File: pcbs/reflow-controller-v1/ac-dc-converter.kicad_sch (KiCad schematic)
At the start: 22 parts, among them U201 TPS62933DRLR

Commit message: footprint assignement fixed; buzzer added
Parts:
- C201: footprint (none) -> Capacitor_SMD:C_0603_1608Metric
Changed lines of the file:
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@@
 			)
 		)
-		(property "Footprint" ""
+		(property "Footprint" "Capacitor_SMD:C_0603_1608Metric"
 			(at 141.9352 43.18 0)
 			(effects

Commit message: WIP pcb design & routing
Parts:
- added D1: SMAJ5.0CA, Diode_SMD:D_SMA, symbol Device:D_TVS
- added J2: PinHeader 1x02 P2.54mm, Connector_PinHeader_2.54mm:PinHeader_1x02_P2.54mm_Vertical, symbol Connector_Generic:Conn_01x02
- added Q1: PMV65XP, Package_TO_SOT_SMD:SOT-23, symbol Device:Q_PMOS_GSD
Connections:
- net +5V: now also Q1.2 (S)
- net GND: now also D1.1 (A1), J2.2 (Pin_2), Q1.1 (G)
- new net: D1.2 (A2), J2.1 (Pin_1), Q1.3 (D)
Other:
- note added: "Debug Power In"

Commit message: update debug power footprint
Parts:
- J2: footprint Connector_PinHeader_2.54mm:PinHeader_1x02_P2.54mm_Vertical -> Connector_Molex:Molex_KK-254_AE-6410-02A_1x02_P2.54mm_Vertical
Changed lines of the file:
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@@
 			)
 		)
-		(property "Footprint" "Connector_PinHeader_2.54mm:PinHeader_1x02_P2.54mm_Vertical"
+		(property "Footprint" "Connector_Molex:Molex_KK-254_AE-6410-02A_1x02_P2.54mm_Vertical"
 			(at 43.18 160.02 0)
 			(effects

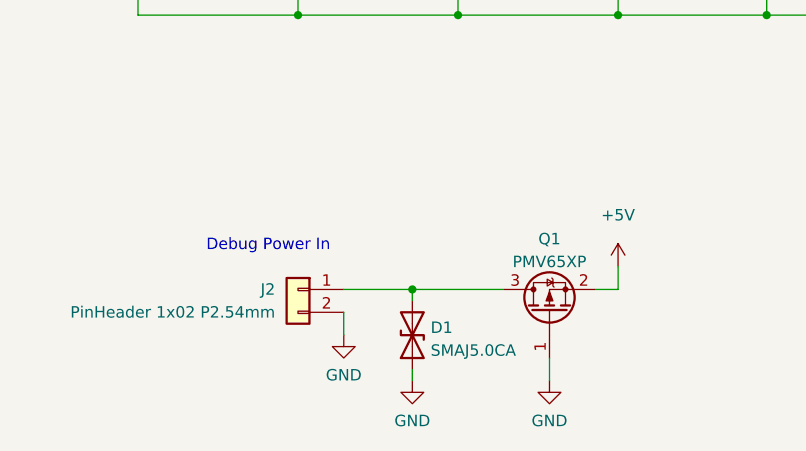
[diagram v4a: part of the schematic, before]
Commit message: add zero crossing detector
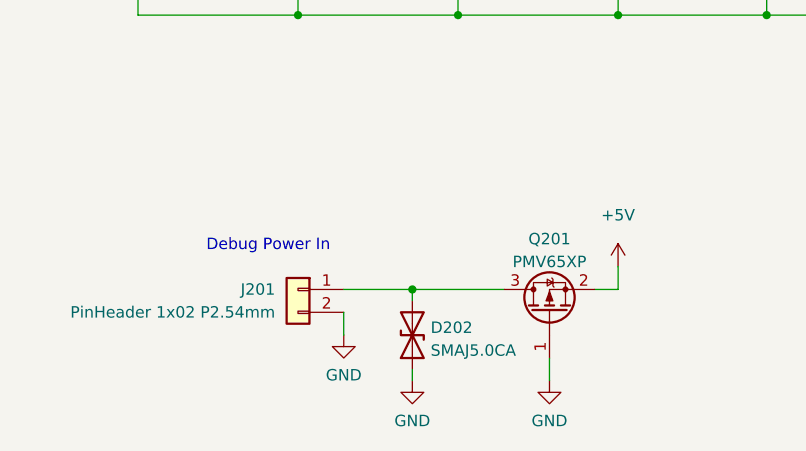
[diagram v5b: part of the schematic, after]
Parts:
- renumbered D1 to D202, J2 to J201, Q1 to Q201

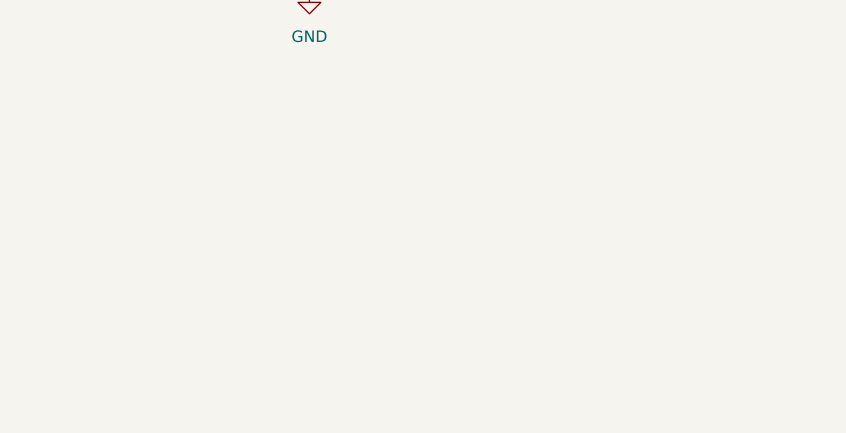
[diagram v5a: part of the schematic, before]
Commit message: add ldo for analog voltage
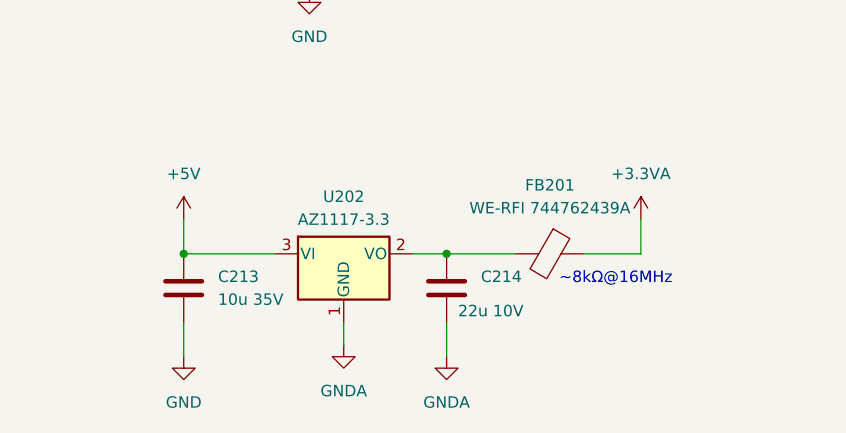
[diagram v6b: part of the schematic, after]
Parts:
- added C213: 10u 35V, Capacitor_SMD:C_1206_3216Metric, symbol Device:C
- added C214: 22u 10V, Capacitor_SMD:C_1206_3216Metric, symbol Device:C
- added FB201: WE-RFI 744762439A, Inductor_SMD:L_1008_2520Metric, symbol Device:FerriteBead
- added U202: AZ1117-3.3, Package_TO_SOT_SMD:SOT-223-3_TabPin2, symbol Regulator_Linear:AZ1117-3.3
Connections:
- net +5V: now also C213.1, U202.3 (VI)
- net GND: now also C213.2
- new net: C214.1, FB201.2, U202.2 (VO)
- new net +3.3VA: FB201.1
- new net GNDA: C214.2, U202.1 (GND)
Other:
- note added: "~8kΩ@16MHz"

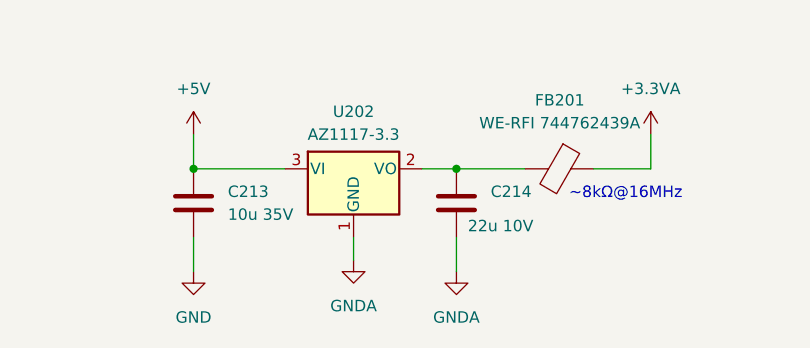
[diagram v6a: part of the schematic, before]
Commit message: update analog voltage ldo placement&routing
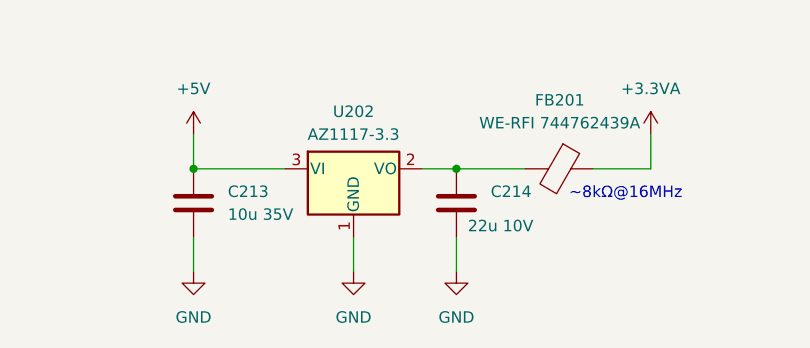
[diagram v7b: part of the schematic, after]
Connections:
- net GNDA is gone; now on net GND: C214.2, U202.1 (GND)
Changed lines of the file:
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@@
 	(wire
 		(pts
-			(xy 130.81 168.91) (xy 130.81 171.45)
+			(xy 130.81 168.91) (xy 130.81 172.72)
 		)
 		(stroke
@@
 	)
 	(symbol
-		(lib_id "power:GNDA")
-		(at 142.24 172.72 0)
-		(unit 1)
-		(exclude_from_sim no)
-		(in_bom yes)
-		(on_board yes)
-		(dnp no)
-		(fields_autoplaced yes)
-		(property "Reference" "#PWR0211"
-			(at 142.24 179.07 0)
-			(effects
-				(font
-					(size 1.27 1.27)
-				)
-				(hide yes)
-			)
-		)
-		(property "Value" "GNDA"
-			(at 142.24 177.8 0)
-			(effects
-				(font
-					(size 1.27 1.27)
-				)
-			)
-		)
-		(property "Footprint" ""
-			(at 142.24 172.72 0)
-			(effects
-				(font
-					(size 1.27 1.27)
-				)
-				(hide yes)
-			)
-		)
-		(property "Datasheet" ""
-			(at 142.24 172.72 0)
-			(effects
-				(font
-					(size 1.27 1.27)
-				)
-				(hide yes)
-			)
-		)
-		(property "Description" "Power symbol creates a global label with name \"GNDA\" , analog ground"
-			(at 142.24 172.72 0)
-			(effects
-				(font
-					(size 1.27 1.27)
-				)
-				(hide yes)
-			)
-		)
-		(pin "1"
-		)
-		(instances
-			(project ""
-				(path "/843848ae-bf49-42cb-8f8b-76790d2e568d/f26231fc-8139-4c10-96b5-ac7abb012bd7"
-					(reference "#PWR0211")
-					(unit 1)
-				)
-			)
-		)
-	)
-	(symbol
 		(lib_id "Regulator_Switching:TPS62933")
 		(at 127 99.06 0)
@@
 	)
 	(symbol
-		(lib_id "power:GNDA")
-		(at 130.81 171.45 0)
-		(unit 1)
-		(exclude_from_sim no)
-		(in_bom yes)
-		(on_board yes)
-		(dnp no)
-		(fields_autoplaced yes)
-		(property "Reference" "#PWR0207"
-			(at 130.81 177.8 0)
-			(effects
-				(font
-					(size 1.27 1.27)
-				)
-				(hide yes)
-			)
-		)
-		(property "Value" "GNDA"
-			(at 130.81 176.53 0)
-			(effects
-				(font
-					(size 1.27 1.27)
-				)
-			)
-		)
-		(property "Footprint" ""
-			(at 130.81 171.45 0)
-			(effects
-				(font
-					(size 1.27 1.27)
-				)
-				(hide yes)
-			)
-		)
-		(property "Datasheet" ""
-			(at 130.81 171.45 0)
-			(effects
-				(font
-					(size 1.27 1.27)
-				)
-				(hide yes)
-			)
-		)
-		(property "Description" "Power symbol creates a global label with name \"GNDA\" , analog ground"
-			(at 130.81 171.45 0)
-			(effects
-				(font
-					(size 1.27 1.27)
-				)
-				(hide yes)
-			)
-		)
-		(pin "1"
-		)
-		(instances
-			(project "reflow-controller-v1"
-				(path "/843848ae-bf49-42cb-8f8b-76790d2e568d/f26231fc-8139-4c10-96b5-ac7abb012bd7"
-					(reference "#PWR0207")
-					(unit 1)
-				)
-			)
-		)
-	)
-	(symbol
 		(lib_id "Device:C")
 		(at 146.05 91.44 90)
@@
 	)
 	(symbol
+		(lib_name "GND_3")
+		(lib_id "power:GND")
+		(at 130.81 172.72 0)
+		(unit 1)
+		(exclude_from_sim no)
+		(in_bom yes)
+		(on_board yes)
+		(dnp no)
+		(fields_autoplaced yes)
+		(property "Reference" "#PWR0207"
+			(at 130.81 179.07 0)
+			(effects
+				(font
+					(size 1.27 1.27)
+				)
+				(hide yes)
+			)
+		)
+		(property "Value" "GND"
+			(at 130.81 177.8 0)
+			(effects
+				(font
+					(size 1.27 1.27)
+				)
+			)
+		)
+		(property "Footprint" ""
+			(at 130.81 172.72 0)
+			(effects
+				(font
+					(size 1.27 1.27)
+				)
+				(hide yes)
+			)
+		)
+		(property "Datasheet" ""
+			(at 130.81 172.72 0)
+			(effects
+				(font
+					(size 1.27 1.27)
+				)
+				(hide yes)
+			)
+		)
+		(property "Description" "Power symbol creates a global label with name \"GND\" , ground"
+			(at 130.81 172.72 0)
+			(effects
+				(font
+					(size 1.27 1.27)
+				)
+				(hide yes)
+			)
+		)
+		(pin "1"
+		)
+		(instances
+			(project "reflow-controller-v1"
+				(path "/843848ae-bf49-42cb-8f8b-76790d2e568d/f26231fc-8139-4c10-96b5-ac7abb012bd7"
+					(reference "#PWR0207")
+					(unit 1)
+				)
+			)
+		)
+	)
+	(symbol
 		(lib_id "Regulator_Linear:AZ1117-3.3")
 		(at 130.81 161.29 0)
@@
 					(unit 1)
 				)
+			)
+		)
+	)
+	(symbol
+		(lib_name "GND_3")
+		(lib_id "power:GND")
+		(at 142.24 172.72 0)
+		(unit 1)
+		(exclude_from_sim no)
+		(in_bom yes)
+		(on_board yes)
+		(dnp no)
+		(fields_autoplaced yes)
+		(property "Reference" "#PWR0210"
+			(at 142.24 179.07 0)
+			(effects
+				(font
+					(size 1.27 1.27)
+				)
+				(hide yes)
+			)
+		)
+		(property "Value" "GND"
+			(at 142.24 177.8 0)
+			(effects
+				(font
+					(size 1.27 1.27)
+				)
+			)
+		)
+		(property "Footprint" ""
+			(at 142.24 172.72 0)
+			(effects
+				(font
+					(size 1.27 1.27)
+				)
+				(hide yes)
+			)
+		)
+		(property "Datasheet" ""
+			(at 142.24 172.72 0)
+			(effects
+				(font
+					(size 1.27 1.27)
+				)
+				(hide yes)
+			)
+		)
+		(property "Description" "Power symbol creates a global label with name \"GND\" , ground"
+			(at 142.24 172.72 0)
+			(effects
+				(font
+					(size 1.27 1.27)
+				)
+				(hide yes)
+			)
+		)
+		(pin "1"
+		)
+		(instances
+			(project "reflow-controller-v1"
+				(path "/843848ae-bf49-42cb-8f8b-76790d2e568d/f26231fc-8139-4c10-96b5-ac7abb012bd7"
+					(reference "#PWR0210")
+					(unit 1)
+				)
